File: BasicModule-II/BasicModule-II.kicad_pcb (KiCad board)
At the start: 2 copper layers, 17.8 x 24.4 mm, 9 parts, among them P1 CONN_01X03, SW1 Pulsador, SW2 Final_carrera

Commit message: Logo atomo añadido
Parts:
- removed the G*** at (137.9, 105.0)
- added G***: LOGO, Grape:atom_small, B.Cu at (137.9, 106.9)
- moved G*** 16.9 mm to (137.8, 91.8)
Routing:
- net SIGNAL: track 31.1 -> 32.4 mm

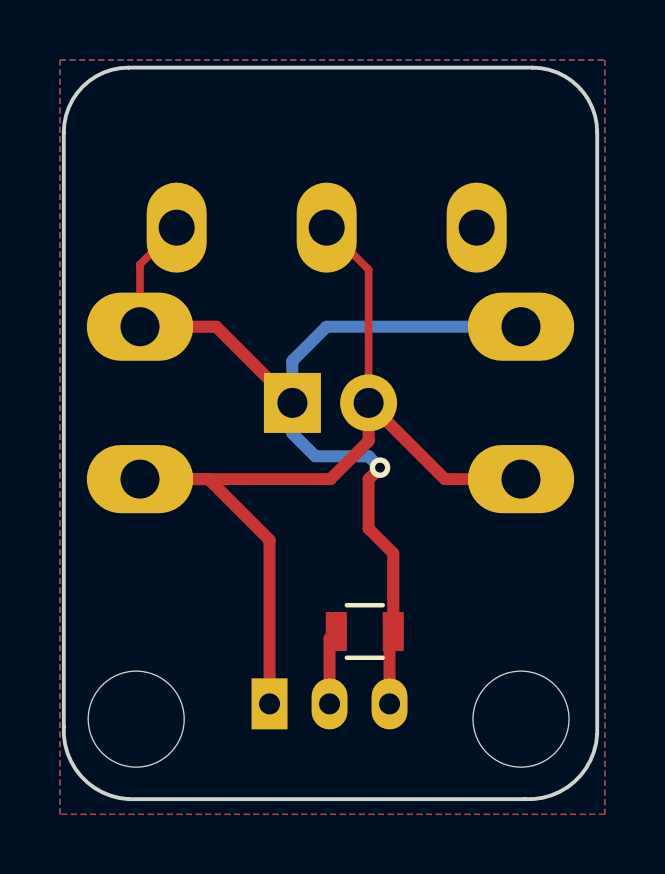
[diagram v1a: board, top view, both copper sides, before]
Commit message: Conector cambiado
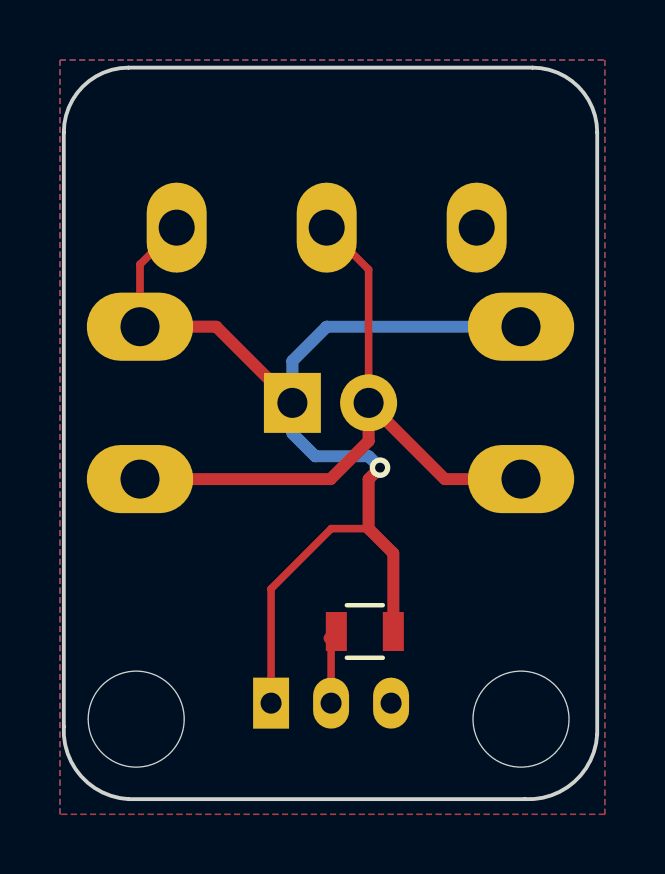
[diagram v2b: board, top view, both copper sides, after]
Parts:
- moved P1 0.06 mm to (135.9, 111.4)
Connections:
- P1 pad 1: GND -> SIGNAL
- P1 pad 3: SIGNAL -> GND
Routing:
- net GND: track 33.2 -> 22.6 mm
- net SIGNAL: track 32.4 -> 38.0 mm
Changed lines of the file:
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@@
     (thickness 1.6)
     (drawings 10)
-    (tracks 34)
+    (tracks 33)
     (zones 0)
     (modules 9)
@@
   )
   (setup
-    (last_trace_width 0.4)
+    (last_trace_width 0.254)
     (user_trace_width 0.1524)
     (user_trace_width 0.2)
@@
   )
   (module Connectors_JST:JST_PH_S3B-PH-K_03x2.00mm_Angled (layer F.Cu)
-    (at 135.89 111.379)
+    (at 135.9408 111.3536)
     (descr http://www.jst-mfg.com/product/pdf/eng/ePH.pdf)
     (tags "connector jst ph")
@@
     (fp_line (start 6.45 6.75) (end -2.45 6.75) (layer Dwgs.User) (width 0.05))
     (pad 1 thru_hole rect (at 0 0) (size 1.2 1.7) (drill 0.7) (layers *.Cu *.Mask)
-      (net 1 GND))
+      (net 2 SIGNAL))
     (pad 2 thru_hole oval (at 2 0) (size 1.2 1.7) (drill 0.7) (layers *.Cu *.Mask)
       (net 3 5V))
     (pad 3 thru_hole oval (at 4 0) (size 1.2 1.7) (drill 0.7) (layers *.Cu *.Mask)
-      (net 2 SIGNAL))
+      (net 1 GND))
   )
   (module Resistors_SMD:R_0805 (layer F.Cu)
@@
   (segment (start 139.192 101.346) (end 139.192 96.901) (width 0.254) (layer F.Cu) (net 1))
   (segment (start 139.192 96.901) (end 137.795 95.504) (width 0.254) (layer F.Cu) (net 1))
-  (segment (start 135.89 111.379) (end 135.89 105.918) (width 0.4) (layer F.Cu) (net 1))
-  (segment (start 133.858 103.886) (end 131.572 103.886) (width 0.4) (layer F.Cu) (net 1))
-  (segment (start 135.89 105.918) (end 133.858 103.886) (width 0.4) (layer F.Cu) (net 1))
   (segment (start 131.572 103.886) (end 137.922 103.886) (width 0.4) (layer F.Cu) (net 1))
   (segment (start 139.192 102.616) (end 139.192 101.346) (width 0.4) (layer F.Cu) (net 1))
@@
   (segment (start 141.732 103.886) (end 139.192 101.346) (width 0.4) (layer F.Cu) (net 1))
   (segment (start 131.572 103.886) (end 132.207 103.886) (width 0.254) (layer F.Cu) (net 1))
+  (segment (start 135.9408 111.3536) (end 135.9408 107.5436) (width 0.254) (layer F.Cu) (net 2) (status 400000))
+  (segment (start 137.9474 105.537) (end 139.192 105.537) (width 0.254) (layer F.Cu) (net 2))
+  (segment (start 135.9408 107.5436) (end 137.9474 105.537) (width 0.254) (layer F.Cu) (net 2))
   (segment (start 140.015 108.966) (end 140.015 106.36) (width 0.4) (layer F.Cu) (net 2))
   (segment (start 136.652 102.362) (end 136.652 101.346) (width 0.4) (layer B.Cu) (net 2))
@@
   (segment (start 131.572 98.806) (end 131.572 96.727) (width 0.254) (layer F.Cu) (net 2))
   (segment (start 131.572 96.727) (end 132.795 95.504) (width 0.254) (layer F.Cu) (net 2))
-  (segment (start 139.89 111.379) (end 139.89 109.091) (width 0.4) (layer F.Cu) (net 2))
   (segment (start 139.89 109.091) (end 140.015 108.966) (width 0.4) (layer F.Cu) (net 2))
   (segment (start 136.652 101.346) (end 136.652 99.949) (width 0.4) (layer B.Cu) (net 2))
@@
   (segment (start 134.112 98.806) (end 136.652 101.346) (width 0.4) (layer F.Cu) (net 2))
   (segment (start 139.89 109.091) (end 140.015 108.966) (width 0.254) (layer F.Cu) (net 2))
-  (segment (start 137.89 111.379) (end 137.89 109.191) (width 0.4) (layer F.Cu) (net 3))
+  (segment (start 137.9408 111.3536) (end 137.9408 109.1402) (width 0.254) (layer F.Cu) (net 3) (status C00000))
+  (segment (start 137.9408 109.1402) (end 138.115 108.966) (width 0.254) (layer F.Cu) (net 3) (status C00000))
   (segment (start 137.89 109.191) (end 138.115 108.966) (width 0.4) (layer F.Cu) (net 3))
   (segment (start 137.89 109.191) (end 138.115 108.966) (width 0.254) (layer F.Cu) (net 3))
-  (segment (start 138.144 111.22) (end 138.144 111.379) (width 0.254) (layer F.Cu) (net 3))
   (zone (net 1) (net_name GND) (layer B.Cu) (hatch edge 0.508)
     (connect_pads (clearance 0.2))

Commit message: Logo girado
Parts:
- turned G*** to 180 degrees
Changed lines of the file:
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@@
   )
   (module Grape:atom_small (layer B.Cu)
-    (at 137.922 106.934)
-    (fp_text reference G*** (at 0 0) (layer B.SilkS) hide
+    (at 137.922 106.934 180)
+    (fp_text reference G*** (at 0 0 180) (layer B.SilkS) hide
       (effects (font (thickness 0.3)) (justify mirror))
     )
-    (fp_text value LOGO (at 0.75 0) (layer B.SilkS) hide
+    (fp_text value LOGO (at 0.75 0 180) (layer B.SilkS) hide
       (effects (font (thickness 0.3)) (justify mirror))
     )
@@
   (segment (start 141.732 103.886) (end 139.192 101.346) (width 0.4) (layer F.Cu) (net 1))
   (segment (start 131.572 103.886) (end 132.207 103.886) (width 0.254) (layer F.Cu) (net 1))
-  (segment (start 135.9408 111.3536) (end 135.9408 107.5436) (width 0.254) (layer F.Cu) (net 2) (status 400000))
+  (segment (start 135.9408 111.3536) (end 135.9408 107.5436) (width 0.254) (layer F.Cu) (net 2))
   (segment (start 137.9474 105.537) (end 139.192 105.537) (width 0.254) (layer F.Cu) (net 2))
   (segment (start 135.9408 107.5436) (end 137.9474 105.537) (width 0.254) (layer F.Cu) (net 2))
@@
   (segment (start 134.112 98.806) (end 136.652 101.346) (width 0.4) (layer F.Cu) (net 2))
   (segment (start 139.89 109.091) (end 140.015 108.966) (width 0.254) (layer F.Cu) (net 2))
-  (segment (start 137.9408 111.3536) (end 137.9408 109.1402) (width 0.254) (layer F.Cu) (net 3) (status C00000))
-  (segment (start 137.9408 109.1402) (end 138.115 108.966) (width 0.254) (layer F.Cu) (net 3) (status C00000))
+  (segment (start 137.9408 111.3536) (end 137.9408 109.1402) (width 0.254) (layer F.Cu) (net 3))
+  (segment (start 137.9408 109.1402) (end 138.115 108.966) (width 0.254) (layer F.Cu) (net 3))
   (segment (start 137.89 109.191) (end 138.115 108.966) (width 0.4) (layer F.Cu) (net 3))
   (segment (start 137.89 109.191) (end 138.115 108.966) (width 0.254) (layer F.Cu) (net 3))
